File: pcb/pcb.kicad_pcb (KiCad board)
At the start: 2 copper layers, 99.9 x 87 mm, 128 parts, among them SW1 SW_Push, SW2 SW_Push, SW3 SW_Push

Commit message: placed and routed LED R0C3
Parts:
- moved D31 118.1 mm to (127.2, 116.8), turned to 105 degrees
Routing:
- net /Row0: track 7.03 -> 7.09 mm, vias 3 -> 4
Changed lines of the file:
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@@
 	(footprint "pcb:XL-0201"
 		(layer "F.Cu")
-		(at 14.09891 150.818166 90)
+		(at 127.196593 116.774118 105)
 		(descr "LED SMD 0.7 mm x 0.4 mm, XINGLIGHT XL-0201 series")
 		(tags "LED")
 		(property "Reference" "D31"
-			(at 0 -1 90)
+			(at 0 -1 105)
 			(layer "F.SilkS")
 			(hide yes)
@@
 		)
 		(property "Value" "LED_Small"
-			(at 0 1 90)
+			(at 0 1 105)
 			(layer "F.Fab")
 			(effects
@@
 		)
 		(property "Datasheet" ""
-			(at 0 0 90)
+			(at 0 0 105)
 			(layer "F.Fab")
 			(hide yes)
@@
 		)
 		(property "Description" "Light emitting diode, small symbol"
-			(at 0 0 90)
+			(at 0 0 105)
 			(layer "F.Fab")
 			(hide yes)
@@
 		)
 		(property "KiLib_Generator" "SMD_2terminal_chip_molded"
-			(at 0 0 90)
+			(at 0 0 105)
 			(layer "F.SilkS")
 			(hide yes)
@@
 		)
 		(property "Sim.Pins" "1=K 2=A"
-			(at 0 0 90)
+			(at 0 0 105)
 			(unlocked yes)
 			(layer "F.Fab")
@@
 		)
 		(property "LCSC" "C965789"
-			(at 0 0 90)
+			(at 0 0 105)
 			(unlocked yes)
 			(layer "F.Fab")
@@
 		)
 		(fp_text user "${REFERENCE}"
-			(at 0 -0.62 90)
+			(at 0 -0.62 105)
 			(layer "F.Fab")
 			(effects
@@
 		)
 		(pad "" smd roundrect
-			(at -0.205 0 90)
+			(at -0.205 0 105)
 			(size 0.15 0.2)
 			(layers "F.Paste")
@@
 		)
 		(pad "" smd roundrect
-			(at 0.205 0 90)
+			(at 0.205 0 105)
 			(size 0.15 0.2)
 			(layers "F.Paste")
@@
 		)
 		(pad "1" smd roundrect
-			(at -0.205 0 90)
+			(at -0.205 0 105)
 			(size 0.17 0.28)
 			(layers "F.Cu" "F.Mask")
@@
 		)
 		(pad "2" smd roundrect
-			(at 0.205 0 90)
+			(at 0.205 0 105)
 			(size 0.17 0.28)
 			(layers "F.Cu" "F.Mask")
@@
 	(gr_curve
 		(pts
+			(xy 127.6 116.5) (xy 127.9 116.3) (xy 128.2 116.1) (xy 127.9 114.2)
+		)
+		(stroke
+			(width 0.1)
+			(type default)
+		)
+		(layer "B.Cu")
+		(net "/Row0")
+	)
+	(gr_curve
+		(pts
+			(xy 127.7 110.5) (xy 126 110.9) (xy 125.6 117.6) (xy 127.6 116.5)
+		)
+		(stroke
+			(width 0.1)
+			(type default)
+		)
+		(layer "B.Cu")
+		(net "/Row0")
+	)
+	(gr_curve
+		(pts
+			(xy 127.9 110.9) (xy 126.6 111.4) (xy 127.1 115) (xy 127.1 116.1)
+		)
+		(stroke
+			(width 0.1)
+			(type default)
+		)
+		(layer "B.Cu")
+		(net "/Col3")
+	)
+	(gr_curve
+		(pts
+			(xy 127.9 114.2) (xy 127.8 113.5) (xy 128.7 113.3) (xy 130.8 112.8)
+		)
+		(stroke
+			(width 0.1)
+			(type default)
+		)
+		(layer "B.Cu")
+		(net "/Row0")
+	)
+	(gr_curve
+		(pts
 			(xy 127.981759 106.7359) (xy 131.9 102.9) (xy 139.1 100.6) (xy 146.941181 98.534074)
 		)
@@
 	(gr_curve
 		(pts
+			(xy 130.8 112.8) (xy 132.5 112.4) (xy 136.1 114.4) (xy 137.1 114.2)
+		)
+		(stroke
+			(width 0.1)
+			(type default)
+		)
+		(layer "B.Cu")
+		(net "/Row0")
+	)
+	(gr_curve
+		(pts
 			(xy 131.1 108.911299) (xy 130.3 108.7) (xy 129.8 108.9) (xy 128.639159 109.189351)
 		)
@@
 	(gr_curve
 		(pts
+			(xy 132.4 108.5) (xy 131.3 109.1) (xy 131 109.9) (xy 127.7 110.5)
+		)
+		(stroke
+			(width 0.1)
+			(type default)
+		)
+		(layer "B.Cu")
+		(net "/Row0")
+	)
+	(gr_curve
+		(pts
 			(xy 132.583561 123.910061) (xy 130.5 124.3) (xy 131.3 122.7) (xy 129.441181 123.434074)
 		)
@@
 	(gr_curve
 		(pts
+			(xy 133.8 109.2) (xy 132.4 110.1) (xy 128.8 110.5) (xy 127.9 110.9)
+		)
+		(stroke
+			(width 0.1)
+			(type default)
+		)
+		(layer "B.Cu")
+		(net "/Col3")
+	)
+	(gr_curve
+		(pts
 			(xy 134.3 124.9) (xy 137.1 124.2) (xy 149.3 124) (xy 150.4 123.3)
 		)
@@
 	(gr_curve
 		(pts
-			(xy 140.6 104.1) (xy 139.4 106.7) (xy 133.4 108.2) (xy 132.4 108.565854)
+			(xy 140.6 104.1) (xy 139.4 106.7) (xy 133.4 107.9) (xy 132.4 108.5)
 		)
 		(stroke
@@
 	(gr_curve
 		(pts
+			(xy 144.6 104.9) (xy 141.9 105.7) (xy 135.2 108.2) (xy 133.8 109.2)
+		)
+		(stroke
+			(width 0.1)
+			(type default)
+		)
+		(layer "B.Cu")
+		(net "/Col3")
+	)
+	(gr_curve
+		(pts
 			(xy 145 66.4) (xy 147.4 66) (xy 155.3 66.5) (xy 159 66.4)
 		)
@@
 	)
 	(segment
+		(start 131.944957 108.755043)
+		(end 132.144957 108.755043)
+		(width 0.1)
+		(layer "F.Cu")
+		(net "/Row0")
+	)
+	(segment
 		(start 140.798015 104.298015)
 		(end 141.046942 104.298015)
@@
 	)
 	(segment
-		(start 131.944957 108.755043)
-		(end 132.4 108.565854)
+		(start 132.144957 108.755043)
+		(end 132.4 108.5)
 		(width 0.1)
 		(layer "F.Cu")
@@
 	)
 	(via
-		(at 132.4 108.565854)
+		(at 132.4 108.5)
+		(size 0.45)
+		(drill 0.3)
+		(layers "F.Cu" "B.Cu")
+		(net "/Row0")
+	)
+	(via
+		(at 127.6 116.5)
 		(size 0.45)
 		(drill 0.3)
@@
 	)
 	(segment
-		(start 153.608109 99.243407)
-		(end 153.601985 99.246942)
-		(width 0.2)
-		(layer "F.Cu")
-		(net "/Col0")
-	)
-	(segment
 		(start 54.098909 165.613167)
 		(end 54.093908 165.618166)
@@
 		(start 153.2 99.1)
 		(end 153.608109 99.243407)
-		(width 0.2)
+		(width 0.1)
 		(layer "F.Cu")
 		(net "/Col0")
@@
 	)
 	(segment
-		(start 153.601985 99.246942)
-		(end 153.605521 99.253066)
-		(width 0.2)
-		(layer "F.Cu")
-		(net "/Col0")
-	)
-	(segment
 		(start 59.098909 165.613167)
 		(end 59.093908 165.618166)
@@
 	)
 	(segment
+		(start 127.143535 116.576103)
+		(end 127.143535 116.143535)
+		(width 0.1)
+		(layer "F.Cu")
+		(net "/Col3")
+	)
+	(segment
 		(start 24.103909 150.618167)
 		(end 24.098908 150.613166)
@@
 	)
 	(segment
+		(start 127.143535 116.143535)
+		(end 127.1 116.1)
+		(width 0.1)
+		(layer "F.Cu")
+		(net "/Col3")
+	)
+	(segment
 		(start 64.093909 150.618166)
 		(end 63.598909 150.618167)
@@
 	)
 	(via
-		(at 14.59891 150.618166)
+		(at 127.1 116.1)
 		(size 0.45)
 		(drill 0.3)

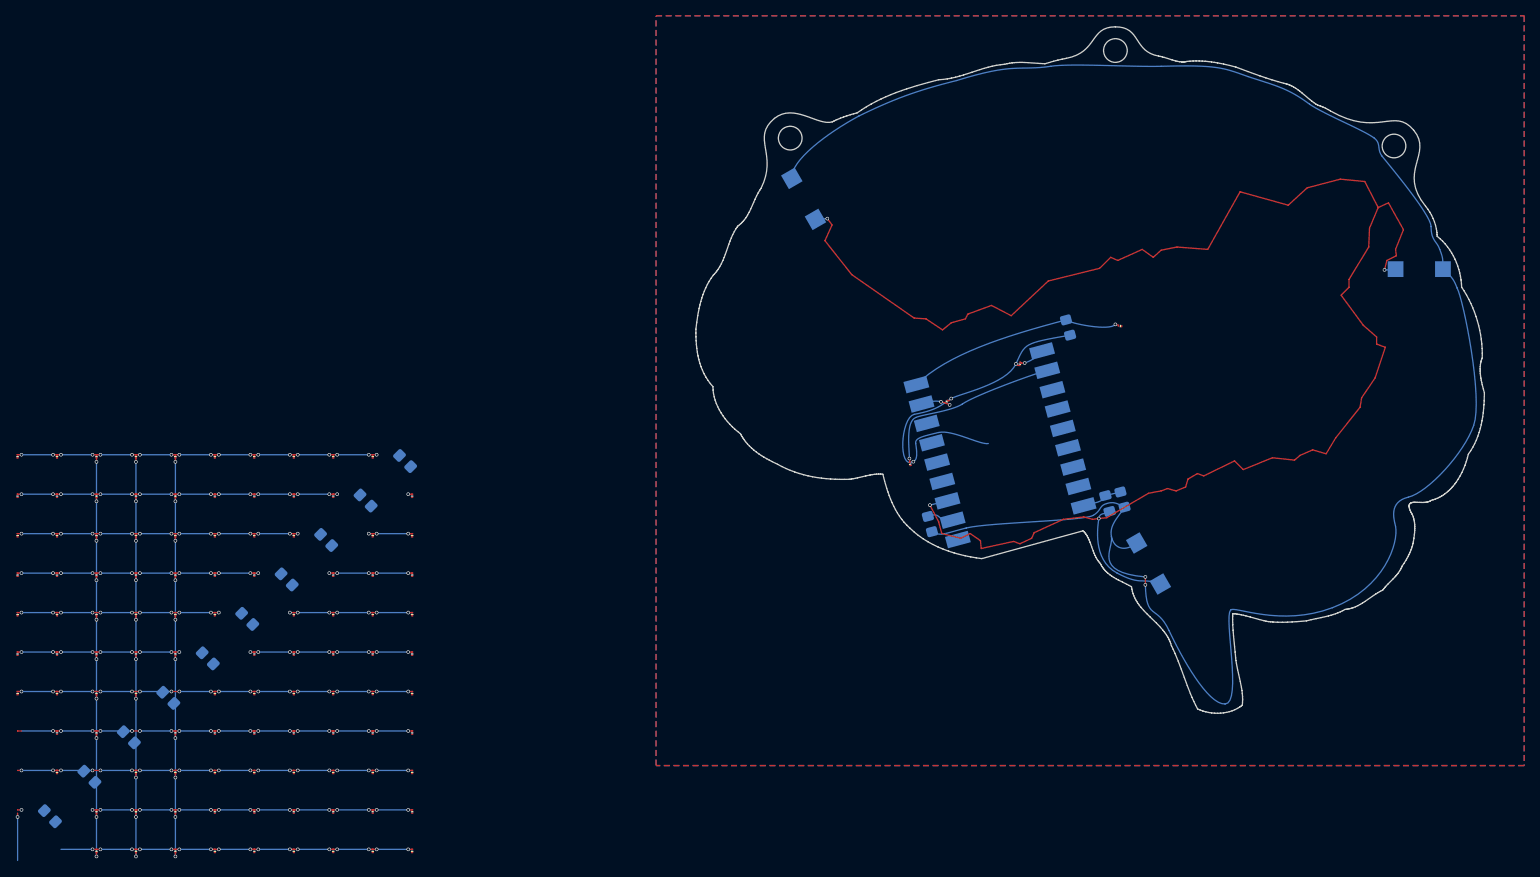
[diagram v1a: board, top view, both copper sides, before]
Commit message: placed remaining parts of row 0 and 1
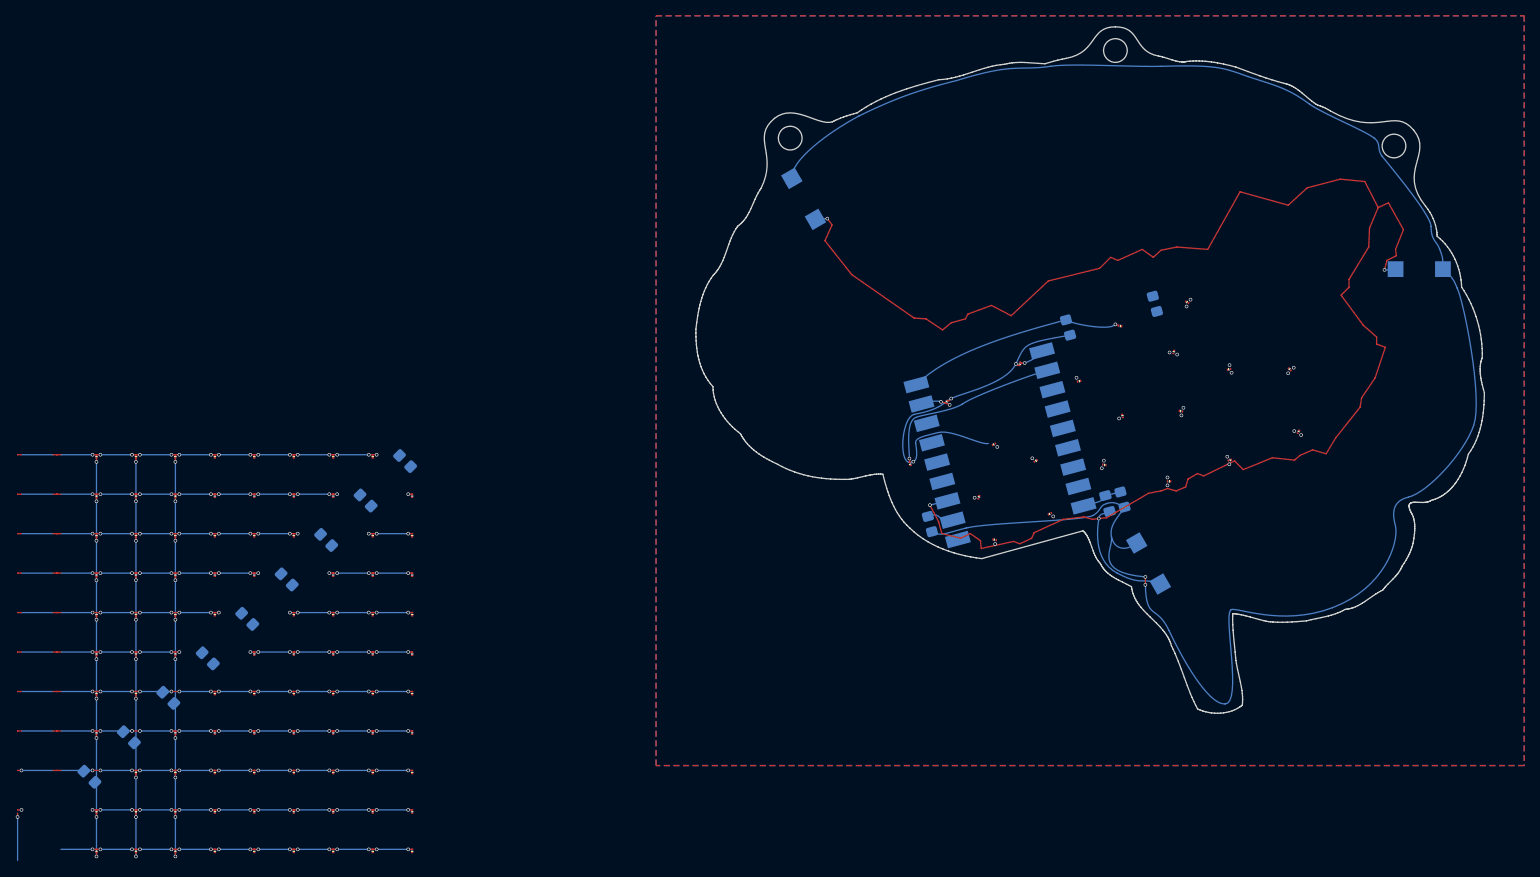
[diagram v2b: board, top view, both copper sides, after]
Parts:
- moved D62 159.3 mm to (175.3, 104.8), turned to -45 degrees
- moved D72 158.3 mm to (176.4, 112.7), turned to -120 degrees
- moved D22 155.1 mm to (162.3, 96.3), turned to -30 degrees
- moved R2 154.3 mm to (158.2, 96.5), turned to -75 degrees
- moved D52 152.8 mm to (167.6, 104.8), turned to 15 degrees
- moved D32 149.5 mm to (160.6, 102.6), turned to -105 degrees
- moved D82 148.9 mm to (167.7, 116.3), turned to -165 degrees
- moved D42 146.8 mm to (161.5, 110.1), turned to -15 degrees
- moved D61 142.2 mm to (154.1, 110.7), turned to -75 degrees
- moved D92 140.9 mm to (160.0, 119.0), turned to 180 degrees
- moved D51 138.9 mm to (148.6, 106.3), turned to -165 degrees
- moved D102 132.7 mm to (151.8, 116.9), turned to 165 degrees
- moved D101 131.0 mm to (144.9, 123.1), turned to 30 degrees
- moved D71 129.8 mm to (143.1, 116.4), turned to -150 degrees
- moved D41 127.7 mm to (137.8, 114.3), turned to 30 degrees
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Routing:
- net /Col9: vias 18 -> 16
- net /Col8: vias 18 -> 17
- net /Col4: vias 20 -> 19
- net +3V3: vias 4 -> 8

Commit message: placed row 3 and 4
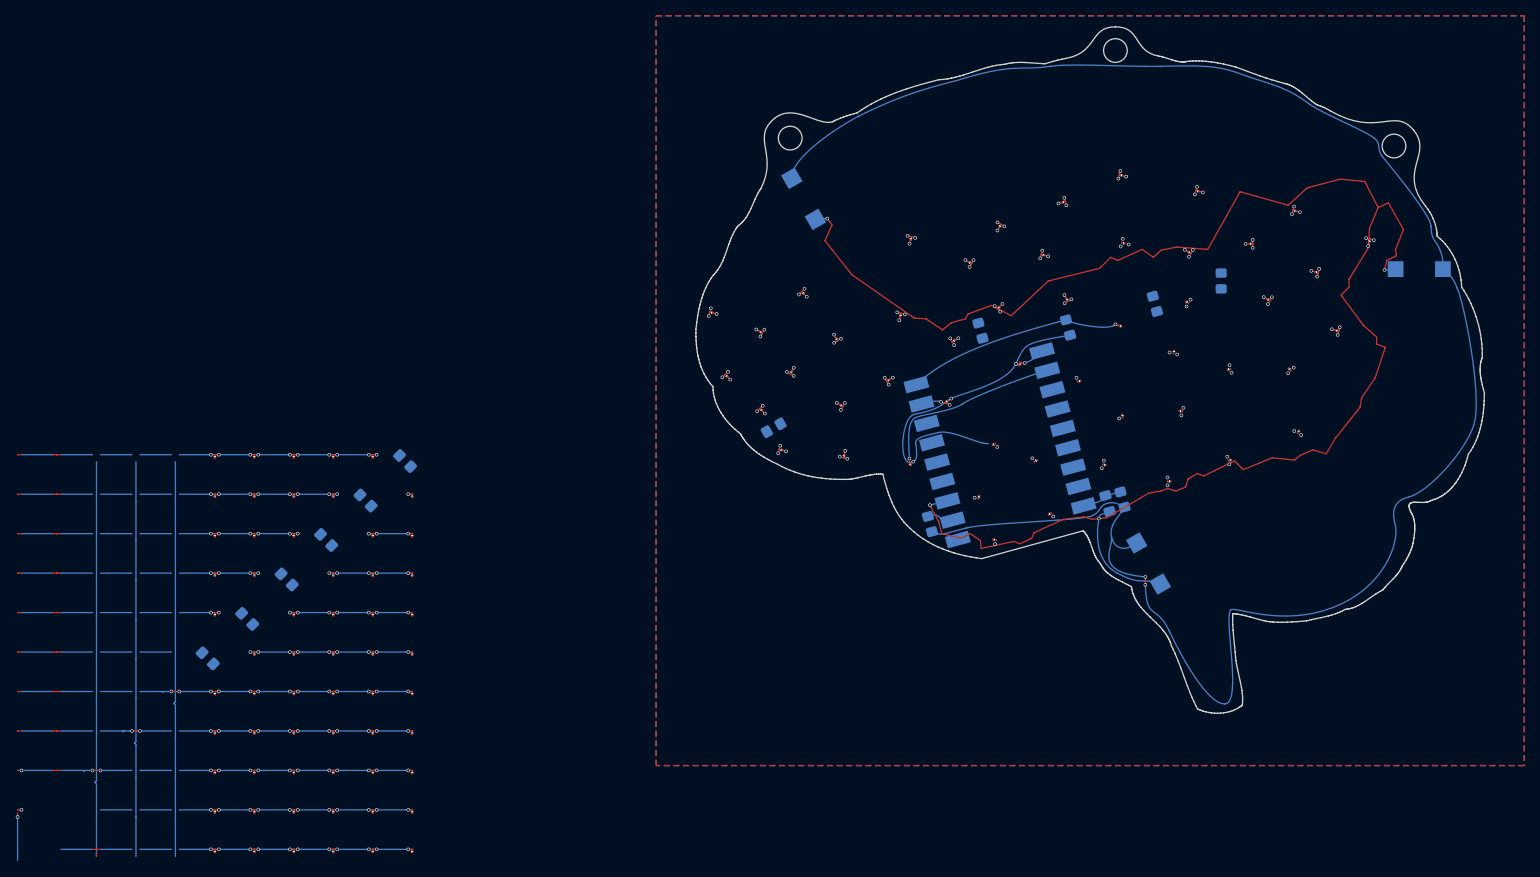
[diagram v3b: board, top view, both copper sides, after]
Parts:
- moved D73 166.8 mm to (185.4, 88.5), turned to 75 degrees
- moved D53 162.0 mm to (178.7, 92.5), turned to -15 degrees
- moved D63 161.3 mm to (181.3, 99.9), turned to -15 degrees
- moved D33 158.9 mm to (170.4, 88.9), turned to 0 degrees
- moved D83 157.3 mm to (175.9, 84.7), turned to 165 degrees
- moved D43 156.6 mm to (172.6, 96.0), turned to -30 degrees
- moved R3 156.6 mm to (166.6, 93.6), turned to 90 degrees
- moved D12 155.6 mm to (162.6, 90.0), turned to -30 degrees
- moved D2 151.2 mm to (154.2, 88.8), turned to 165 degrees
- moved D93 144.7 mm to (163.6, 82.2), turned to 165 degrees
- moved D3 137.1 mm to (147.1, 96.0), turned to -60 degrees
- moved D13 134.8 mm to (144.0, 90.3), turned to 165 degrees
- moved D103 134.6 mm to (153.9, 80.2), turned to 165 degrees
- moved D23 124.1 mm to (138.4, 97.0), turned to -135 degrees
- moved D104 121.9 mm to (146.7, 83.6), turned to 15 degrees
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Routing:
- net /Col9: vias 16 -> 17
- net +3V3: vias 8 -> 7

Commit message: placed row 5 and 6
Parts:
- moved D6 149.8 mm to (156.5, 66.8), turned to 30 degrees
- moved D16 140.8 mm to (151.3, 69.6), turned to 0 degrees
- moved D26 134.8 mm to (145.7, 67.3), turned to 0 degrees
- moved D36 124.1 mm to (136.9, 68.4), turned to 15 degrees
- moved R7 117.6 mm to (141.4, 71.7), turned to -90 degrees
- moved D77 116.8 mm to (144.8, 71.6), turned to 105 degrees
- moved D56 116.2 mm to (138.1, 72.5), turned to 180 degrees
- moved D107 115.6 mm to (152.0, 74.2), turned to -150 degrees
- moved D46 114.0 mm to (129.8, 70.6)
- moved D97 111.7 mm to (147.0, 77.4), turned to -165 degrees
- moved R6 109.9 mm to (125.8, 75.1), turned to 75 degrees
- moved D66 109.5 mm to (130.4, 75.4), turned to -30 degrees
- moved D45 108.8 mm to (121.1, 74.3), turned to 15 degrees
- moved D87 106.7 mm to (139.6, 78.3), turned to 135 degrees
- moved D35 104.5 mm to (115.9, 80.0), turned to 45 degrees
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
